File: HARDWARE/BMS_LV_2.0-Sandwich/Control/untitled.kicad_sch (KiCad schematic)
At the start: 21 parts, among them J3 FTSH-107-01-L-D-K, U1 STM32G484RETx, Y1 ATX-11-F-32.000MHZ-F05-T

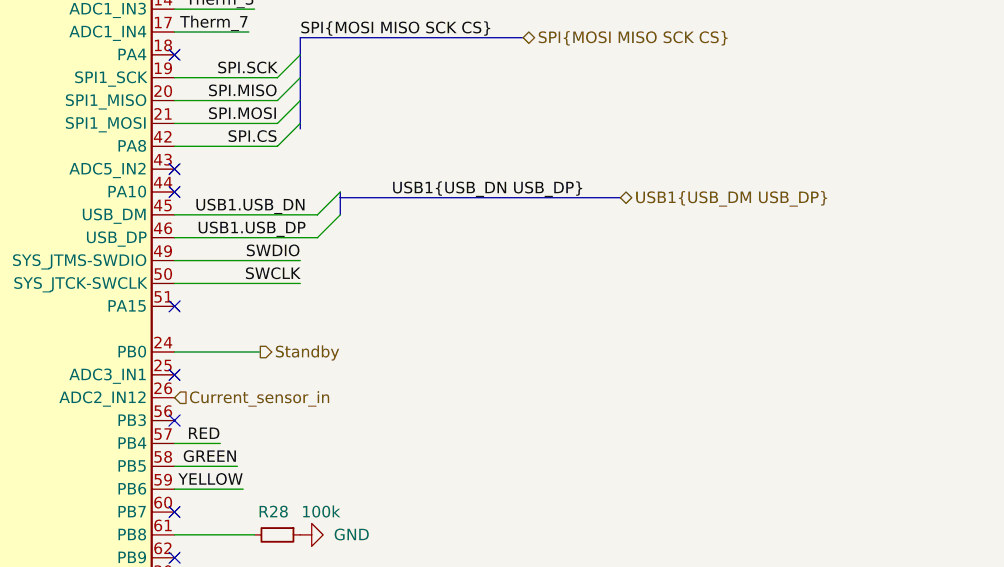
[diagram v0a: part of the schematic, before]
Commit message: Zmieniono złącze programatora na kątowe
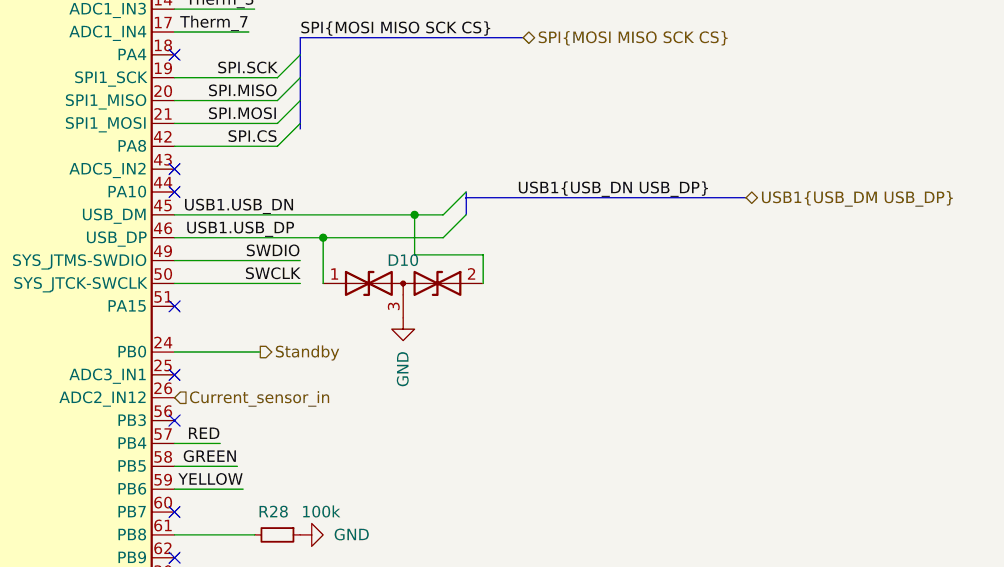
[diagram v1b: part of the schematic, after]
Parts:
- added D10: D_TVS_Dual_AAC, Package_TO_SOT_SMD:SOT-23_Handsoldering, symbol Device:D_TVS_Dual_AAC
- J3: footprint Footprint:FTSH-107-XX-YYY-DV-K -> Footprint:FTSH-107-XX-YYY-DH-TR; Height (none) -> https://www.mouser.pl/ProductDetail/Samtec/FTSH-107-01-L-DH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
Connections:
- net GND: now also D10.3 (common)
- net USB1.USB_DN: now also D10.2 (A2)
- net USB1.USB_DP: now also D10.1 (A1)

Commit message: Poprawnie zrobiony programator
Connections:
- net NRST: now also D7.4 (I/O3); no longer D7.1 (I/O1)
- net SWCLK: now also D8.6 (I/O4); no longer D7.6 (I/O4)
- net SWDIO: now also D8.4 (I/O3); no longer D7.4 (I/O3)
- net SWO: now also D7.3 (I/O2), U1.56 (PB3)
- net URAT_RX: no longer D8.6 (I/O4), U1.52 (PC10)
- net URAT_TX: no longer D8.4 (I/O3), U1.53 (PC11)
- no-connect marks 29 -> 30
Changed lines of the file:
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@@
 	)
 	(no_connect
-		(at 69.215 165.735)
-	)
-	(no_connect
 		(at 173.355 99.695)
 	)
@@
 	)
 	(no_connect
+		(at 69.215 160.655)
+	)
+	(no_connect
 		(at 46.355 161.925)
 	)
@@
 	)
 	(no_connect
+		(at 173.355 114.935)
+	)
+	(no_connect
 		(at 208.915 112.395)
 	)
@@
 	)
 	(no_connect
+		(at 97.155 160.655)
+	)
+	(no_connect
 		(at 208.915 92.075)
 	)
@@
 	)
 	(no_connect
-		(at 186.055 59.055)
+		(at 173.355 117.475)
 	)
 	(no_connect
-		(at 33.655 161.925)
+		(at 186.055 59.055)
 	)
 	(no_connect
-		(at 208.915 117.475)
+		(at 33.655 161.925)
 	)
 	(no_connect
 		(at 208.915 127.635)
 	)
-	(no_connect
-		(at 48.895 169.545)
-	)
 	(bus_entry
 		(at 222.885 79.375)
@@
 		)
 	)
+	(wire
+		(pts
+			(xy 97.155 165.735) (xy 101.6 165.735)
+		)
+		(stroke
+			(width 0)
+			(type default)
+		)
+	)
 	(bus
 		(pts
@@
 	(wire
 		(pts
-			(xy 164.465 114.935) (xy 173.355 114.935)
+			(xy 62.865 165.735) (xy 69.215 165.735)
 		)
 		(stroke
@@
 	(wire
 		(pts
-			(xy 66.04 160.655) (xy 69.215 160.655)
-		)
-		(stroke
-			(width 0)
-			(type default)
-		)
-	)
-	(wire
-		(pts
 			(xy 182.88 50.8) (xy 186.055 50.8)
 		)
@@
 	(wire
 		(pts
-			(xy 164.465 117.475) (xy 173.355 117.475)
-		)
-		(stroke
-			(width 0)
-			(type default)
-		)
-	)
-	(wire
-		(pts
 			(xy 158.75 66.675) (xy 163.83 66.675)
 		)
@@
 	(wire
 		(pts
-			(xy 97.155 165.735) (xy 104.775 165.735)
-		)
-		(stroke
-			(width 0)
-			(type default)
-		)
-	)
-	(wire
-		(pts
 			(xy 225.425 102.235) (xy 225.425 97.155)
 		)
@@
 	(wire
 		(pts
-			(xy 96.52 177.165) (xy 100.965 177.165)
-		)
-		(stroke
-			(width 0)
-			(type default)
-		)
-	)
-	(wire
-		(pts
 			(xy 208.915 122.555) (xy 215.9 122.555)
 		)
@@
 	(wire
 		(pts
+			(xy 208.915 117.475) (xy 213.36 117.475)
+		)
+		(stroke
+			(width 0)
+			(type default)
+		)
+	)
+	(wire
+		(pts
 			(xy 128.27 120.65) (xy 132.08 120.65)
 		)
@@
 	(wire
 		(pts
+			(xy 96.52 179.705) (xy 103.505 179.705)
+		)
+		(stroke
+			(width 0)
+			(type default)
+		)
+	)
+	(wire
+		(pts
 			(xy 208.915 147.955) (xy 214.63 147.955)
 		)
@@
 	(wire
 		(pts
-			(xy 96.52 174.625) (xy 104.775 174.625)
-		)
-		(stroke
-			(width 0)
-			(type default)
-		)
-	)
-	(wire
-		(pts
 			(xy 235.585 94.615) (xy 235.585 99.06)
 		)
@@
 	(wire
 		(pts
+			(xy 96.52 177.165) (xy 102.235 177.165)
+		)
+		(stroke
+			(width 0)
+			(type default)
+		)
+	)
+	(wire
+		(pts
 			(xy 46.355 169.545) (xy 50.165 169.545)
 		)
@@
 	(wire
 		(pts
-			(xy 96.52 179.705) (xy 104.775 179.705)
-		)
-		(stroke
-			(width 0)
-			(type default)
-		)
-	)
-	(wire
-		(pts
 			(xy 188.595 55.245) (xy 191.135 55.245)
 		)
@@
 	(wire
 		(pts
-			(xy 97.155 160.655) (xy 104.775 160.655)
+			(xy 96.52 174.625) (xy 104.14 174.625)
 		)
 		(stroke
@@
 	)
 	(label "SWDIO"
-		(at 104.775 165.735 180)
-		(effects
-			(font
-				(size 1.27 1.27)
-			)
-			(justify right bottom)
-		)
-	)
-	(label "URAT_TX"
-		(at 104.775 179.705 180)
+		(at 103.505 179.705 180)
 		(effects
 			(font
@@
 		)
 	)
-	(label "URAT_RX"
-		(at 104.775 174.625 180)
-		(effects
-			(font
-				(size 1.27 1.27)
-			)
-			(justify right bottom)
-		)
-	)
 	(label "Therm_7"
 		(at 132.08 128.27 0)
@@
 	)
 	(label "NRST"
-		(at 66.04 160.655 180)
+		(at 101.6 165.735 180)
 		(effects
 			(font
@@
 		)
 	)
-	(label "3V3"
-		(at 101.6 163.195 180)
+	(label "SWO"
+		(at 62.865 165.735 0)
 		(effects
 			(font
 				(size 1.27 1.27)
 			)
-			(justify right bottom)
+			(justify left bottom)
 		)
 	)
-	(label "URAT_RX"
-		(at 164.465 114.935 0)
+	(label "3V3"
+		(at 101.6 163.195 180)
 		(effects
 			(font
 				(size 1.27 1.27)
 			)
-			(justify left bottom)
+			(justify right bottom)
 		)
 	)
@@
 		)
 	)
+	(label "SWO"
+		(at 213.36 117.475 180)
+		(effects
+			(font
+				(size 1.27 1.27)
+			)
+			(justify right bottom)
+		)
+	)
 	(label "Therm_2"
 		(at 217.805 69.215 180)
@@
 		)
 	)
-	(label "URAT_TX"
-		(at 164.465 117.475 0)
-		(effects
-			(font
-				(size 1.27 1.27)
-			)
-			(justify left bottom)
-		)
-	)
 	(label "SPI.MISO"
 		(at 220.345 81.915 180)
@@
 	)
 	(label "3V3"
-		(at 100.965 177.165 180)
+		(at 102.235 177.165 180)
 		(effects
 			(font
@@
 	)
 	(label "SWCLK"
-		(at 104.775 160.655 180)
+		(at 104.14 174.625 180)
 		(effects
 			(font

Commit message: Zmieniono tvs, dodano znowu uart, poprawiono silkscreen, gotowy na release
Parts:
- removed D7, D8: Quad TVS, Footprint:SOT65P210X110-6N, symbol D5V0P4UR6SO-7:D5V0P4UR6SO-7
- added D11, D12, D13, D5, D6, D7, D8: SMF3.0, Diode_SMD:D_SOD-123F, symbol Device:D_Zener_Small
- added R27: 100k, Resistor_SMD:R_0603_1608Metric_Pad0.98x0.95mm_HandSolder, symbol Device:R_Small
- added R29: 100, Resistor_SMD:R_0603_1608Metric_Pad0.98x0.95mm_HandSolder, symbol Device:R_Small
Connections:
- net 3V3: now also D6.1 (K), R27.2
- net GND: now also D11.2 (A), D12.2 (A), D13.2 (A), D5.2 (A), D6.2 (A), D7.2 (A), D8.2 (A)
- net Interlock: now also R27.1
- net NRST: now also D7.1 (K), R29.1; no longer U1.7 (PG10)
- net SWCLK: now also D8.1 (K)
- net SWDIO: now also D11.1 (K)
- net SWO: now also D5.1 (K)
- net URAT_RX: now also U1.52 (PC10), D13.1 (K)
- net URAT_TX: now also U1.53 (PC11), D12.1 (K)
- new net: R29.2, U1.7 (PG10)
- no-connect marks 30 -> 25
